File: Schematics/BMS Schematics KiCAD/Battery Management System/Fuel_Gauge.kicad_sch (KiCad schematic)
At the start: 30 parts, among them Q18 2N7002, Q19 BSS84, Q20 2N7002, SW3 SW_Push, U5 BQ34Z100PWR-R2

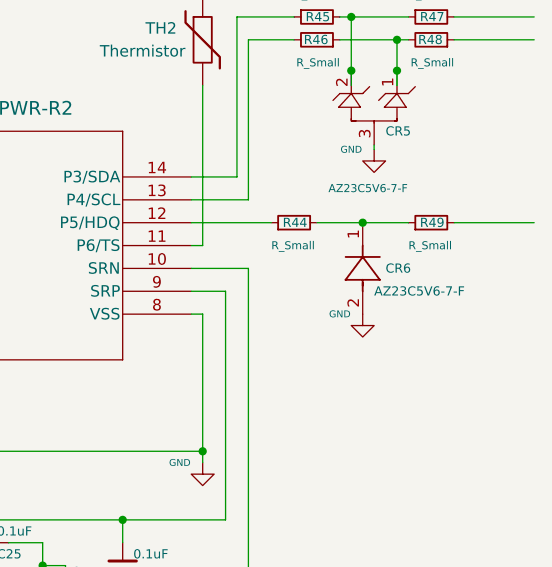
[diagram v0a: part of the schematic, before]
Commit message: Add files via upload
Latest iteration of KiCAD schematic for Battery Management System
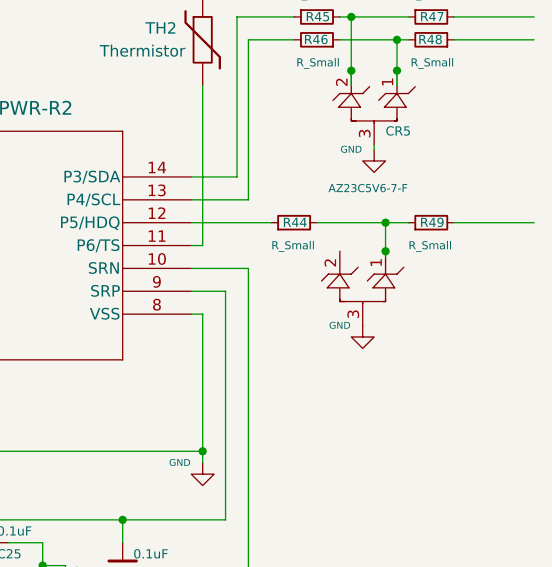
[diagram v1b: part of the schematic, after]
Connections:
- net GND: now also CR6.3; no longer CR6.2
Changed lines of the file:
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@@
 	)
 	(junction
-		(at 149.86 53.34)
-		(diameter 0)
-		(color 0 0 0 0)
-	)
-	(junction
 		(at 50.8 33.02)
 		(diameter 0)
@@
 	)
 	(junction
+		(at 152.4 53.34)
+		(diameter 0)
+		(color 0 0 0 0)
+	)
+	(junction
 		(at 101.6 93.98)
 		(diameter 0)
@@
 	)
 	(junction
+		(at 152.4 56.515)
+		(diameter 0)
+		(color 0 0 0 0)
+	)
+	(junction
 		(at 90.17 88.9)
 		(diameter 0)
@@
 	(wire
 		(pts
+			(xy 152.4 56.515) (xy 152.4 57.15)
+		)
+		(stroke
+			(width 0)
+			(type default)
+		)
+	)
+	(wire
+		(pts
 			(xy 130.81 48.26) (xy 135.89 48.26)
 		)
@@
 	(wire
 		(pts
-			(xy 144.78 53.34) (xy 149.86 53.34)
+			(xy 144.78 53.34) (xy 152.4 53.34)
 		)
 		(stroke
@@
 	(wire
 		(pts
+			(xy 152.4 53.34) (xy 152.4 56.515)
+		)
+		(stroke
+			(width 0)
+			(type default)
+		)
+	)
+	(wire
+		(pts
 			(xy 110.49 93.98) (xy 114.3 93.98)
 		)
@@
 	(wire
 		(pts
-			(xy 149.86 53.34) (xy 154.94 53.34)
-		)
-		(stroke
-			(width 0)
-			(type default)
-		)
-	)
-	(wire
-		(pts
 			(xy 39.37 33.02) (xy 39.37 44.45)
 		)
@@
 	(wire
 		(pts
+			(xy 152.4 53.34) (xy 154.94 53.34)
+		)
+		(stroke
+			(width 0)
+			(type default)
+		)
+	)
+	(wire
+		(pts
 			(xy 132.08 55.88) (xy 130.81 55.88)
 		)
@@
 		(lib_name "AZ23C5V6-7-F_1")
 		(lib_id "AZ23C5V6-7-F:AZ23C5V6-7-F")
-		(at 149.86 63.5 90)
+		(at 148.59 64.77 90)
 		(unit 1)
 		(exclude_from_sim no)
@@
 		(dnp no)
 		(property "Reference" "CR6"
-			(at 152.4 58.42 90)
+			(at 151.13 59.69 90)
 			(effects
 				(font
@@
 				)
 				(justify right)
+				(hide yes)
 			)
 		)
 		(property "Value" "AZ23C5V6-7-F"
-			(at 151.13 60.96 90)
+			(at 149.86 62.23 90)
 			(effects
 				(font
@@
 				)
 				(justify right)
+				(hide yes)
 			)
 		)
 		(property "Footprint" "DIODE3_AZ23C5V6-7-F_DIO"
-			(at 149.86 63.5 0)
+			(at 148.59 64.77 0)
 			(effects
 				(font
@@
 		)
 		(property "Datasheet" "AZ23C5V6-7-F"
-			(at 149.86 63.5 0)
+			(at 148.59 64.77 0)
 			(effects
 				(font
@@
 		)
 		(property "Description" ""
-			(at 149.86 63.5 0)
+			(at 148.59 64.77 0)
 			(effects
 				(font
@@
 		(pin "1"
 		)
+		(pin "3"
+		)
 		(instances
 			(project "Battery Management System"
@@
 	(symbol
 		(lib_id "power:GND")
-		(at 149.86 63.5 0)
+		(at 149.86 64.77 0)
 		(mirror y)
 		(unit 1)
@@
 		(dnp no)
 		(property "Reference" "#PWR041"
-			(at 149.86 69.85 0)
+			(at 149.86 71.12 0)
 			(effects
 				(font
@@
 		)
 		(property "Value" "GND"
-			(at 147.32 63.5 0)
+			(at 147.32 64.77 0)
 			(effects
 				(font
@@
 		)
 		(property "Footprint" ""
-			(at 149.86 63.5 0)
+			(at 149.86 64.77 0)
 			(effects
 				(font
@@
 		)
 		(property "Datasheet" ""
-			(at 149.86 63.5 0)
+			(at 149.86 64.77 0)
 			(effects
 				(font
@@
 		)
 		(property "Description" "Power symbol creates a global label with name \"GND\" , ground"
-			(at 149.86 63.5 0)
+			(at 149.86 64.77 0)
 			(effects
 				(font
